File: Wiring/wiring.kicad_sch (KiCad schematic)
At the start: 8 parts, among them M1 Motor_Servo, M2 Motor_Servo, M3 Motor_Servo, M4 Motor_Servo, M5 Motor_Servo

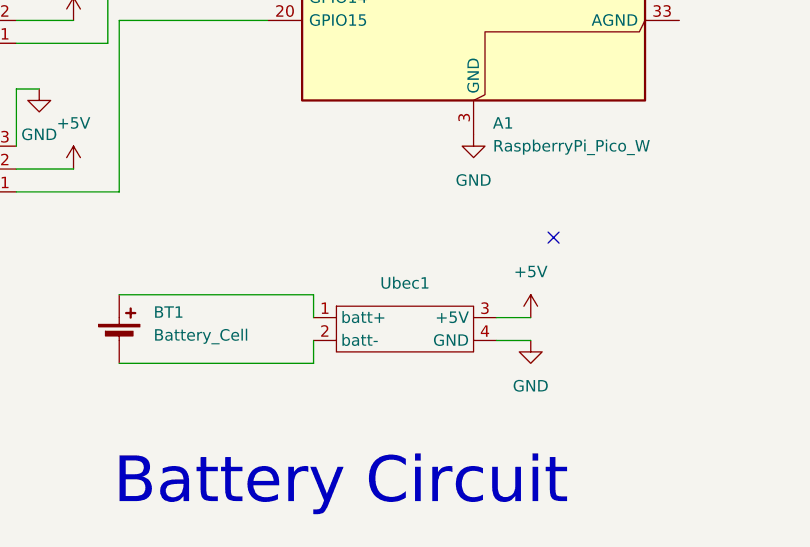
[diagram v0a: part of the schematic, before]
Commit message: wiring updated
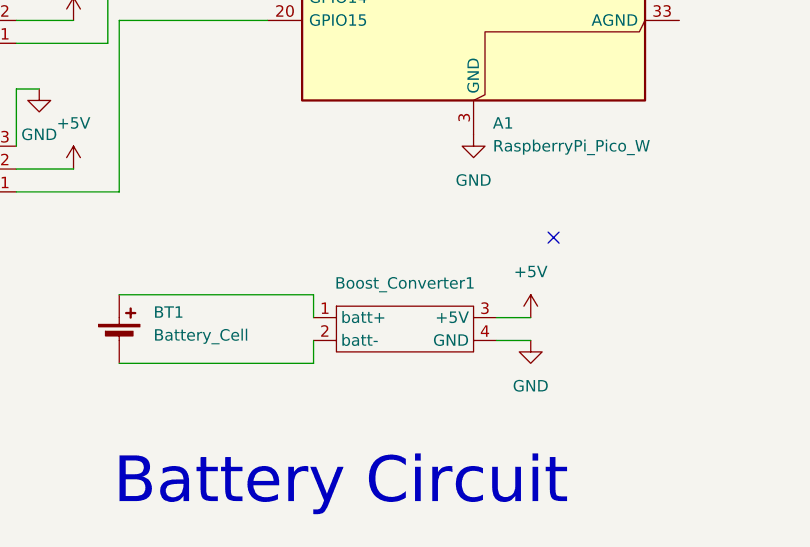
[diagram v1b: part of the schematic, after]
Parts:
- removed Ubec1: (no value), symbol Custom ahh:ubec
- added Boost_Converter1: (no value), symbol Custom ahh:ubec
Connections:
- net +5V: now also Boost_Converter1.3 (+5V)
- net GND: now also Boost_Converter1.4 (GND)
- net at BT1.1 (+): now also Boost_Converter1.1 (batt+)
- net at BT1.2 (-): now also Boost_Converter1.2 (batt-)
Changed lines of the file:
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@@
+	)
+	(symbol
+		(lib_id "Custom ahh:ubec")
+		(at 129.54 157.48 0)
+		(unit 1)
+		(body_style 1)
+		(exclude_from_sim no)
+		(in_bom yes)
+		(on_board yes)
+		(in_pos_files yes)
+		(dnp no)
+		(fields_autoplaced yes)
+		(property "Reference" "Boost_Converter1"
+			(at 129.54 152.4 0)
+			(show_name no)
+			(do_not_autoplace no)
+			(effects
+				(font
+					(size 1.27 1.27)
+				)
+			)
+		)
+		(property "Value" ""
+			(at 129.54 157.48 0)
+			(show_name no)
+			(do_not_autoplace no)
+			(effects
+				(font
+					(size 1.27 1.27)
+				)
+			)
+		)
+		(property "Footprint" ""
+			(at 129.54 157.48 0)
+			(hide yes)
+			(show_name no)
+			(do_not_autoplace no)
+			(effects
+				(font
+					(size 1.27 1.27)
+				)
+			)
+		)
+		(property "Datasheet" ""
+			(at 129.54 157.48 0)
+			(hide yes)
+			(show_name no)
+			(do_not_autoplace no)
+			(effects
+				(font
+					(size 1.27 1.27)
+				)
+			)
+		)
+		(property "Description" ""
+			(at 129.54 157.48 0)
+			(hide yes)
+			(show_name no)
+			(do_not_autoplace no)
+			(effects
+				(font
+					(size 1.27 1.27)
+				)
+			)
+		)
+		(pin "3"
+		)
+		(pin "1"
+		)
+		(pin "4"
+		)
+		(pin "2"
+		)
+		(instances
+			(project "wiring"
+				(path "/25aa3007-d302-4107-a2ee-effaddafa66c"
+					(reference "Boost_Converter1")
+					(unit 1)
+				)
+			)
+		)
 	)
 	(symbol
@@
 					(unit 1)
 				)
-			)
-		)
-	)
-	(symbol
-		(lib_id "Custom ahh:ubec")
-		(at 129.54 157.48 0)
-		(unit 1)
-		(body_style 1)
-		(exclude_from_sim no)
-		(in_bom yes)
-		(on_board yes)
-		(in_pos_files yes)
-		(dnp no)
-		(fields_autoplaced yes)
-		(property "Reference" "Ubec1"
-			(at 129.54 152.4 0)
-			(show_name no)
-			(do_not_autoplace no)
-			(effects
-				(font
-					(size 1.27 1.27)
-				)
-			)
-		)
-		(property "Value" ""
-			(at 129.54 157.48 0)
-			(show_name no)
-			(do_not_autoplace no)
-			(effects
-				(font
-					(size 1.27 1.27)
-				)
-			)
-		)
-		(property "Footprint" ""
-			(at 129.54 157.48 0)
-			(hide yes)
-			(show_name no)
-			(do_not_autoplace no)
-			(effects
-				(font
-					(size 1.27 1.27)
-				)
-			)
-		)
-		(property "Datasheet" ""
-			(at 129.54 157.48 0)
-			(hide yes)
-			(show_name no)
-			(do_not_autoplace no)
-			(effects
-				(font
-					(size 1.27 1.27)
-				)
-			)
-		)
-		(property "Description" ""
-			(at 129.54 157.48 0)
-			(hide yes)
-			(show_name no)
-			(do_not_autoplace no)
-			(effects
-				(font
-					(size 1.27 1.27)
-				)
-			)
-		)
-		(pin "2"
-		)
-		(pin "4"
-		)
-		(pin "3"
-		)
-		(pin "1"
-		)
-		(instances
-			(project "wiring"
-				(path "/25aa3007-d302-4107-a2ee-effaddafa66c"
-					(reference "Ubec1")
-					(unit 1)
-				)
